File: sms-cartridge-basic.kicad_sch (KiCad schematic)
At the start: 5 parts, among them U1 27C256, U2 SMSUCartEdge

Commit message: v0.1
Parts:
- U2: footprint (none) -> MasterSystem:SMS_Cartridge
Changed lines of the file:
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@@
   (no_connect (at 216.535 57.785))
   (no_connect (at 216.535 60.325))
+  (no_connect (at 216.535 83.185))
   (no_connect (at 216.535 75.565))
   (no_connect (at 216.535 78.105))
   (no_connect (at 216.535 80.645))
-  (no_connect (at 216.535 83.185))
   (no_connect (at 216.535 67.945))
   (no_connect (at 216.535 70.485))
@@
       (effects (font (size 1.27 1.27)) (justify left))
     )
-    (property "Footprint" "" (id 2) (at 205.105 52.705 0)
+    (property "Footprint" "MasterSystem:SMS_Cartridge" (id 2) (at 205.105 52.705 0)
       (effects (font (size 1.27 1.27)) hide)
     )
@@
     )
     (path "/cae6533d-13d3-4f9b-a8e3-e699bd050290"
-      (reference "U2") (unit 1) (value "SMSUCartEdge") (footprint "")
-    )
-  )
+      (reference "U2") (unit 1) (value "SMSUCartEdge") (footprint "MasterSystem:SMS_Cartridge")
+    )
+  )

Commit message: Bodge to M0-7
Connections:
- net ~{M0-7}: now reaches U2.11 (~{M0-7})
- net ~{M0-7}: now also U1.22 (~{OE})
- net ~{RD}: no longer names the net of U2.4 (~{RD})
- net ~{RD}: no longer U1.22 (~{OE})
- no-connect marks 16 -> 19
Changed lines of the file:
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@@
   (junction (at 210.185 137.795) (diameter 0) (color 0 0 0 0)
   )
+  (no_connect (at 216.535 106.045))
+  (no_connect (at 216.535 103.505))
+  (no_connect (at 216.535 100.965))
   (no_connect (at 216.535 108.585))
   (no_connect (at 216.535 57.785))
@@
     (stroke (width 0) (type default) (color 0 0 0 0))
   )
+  (wire (pts (xy 216.535 98.425) (xy 222.885 98.425))
+    (stroke (width 0) (type default) (color 0 0 0 0))
+  )
   (wire (pts (xy 196.85 100.965) (xy 198.755 100.965))
     (stroke (width 0) (type default) (color 0 0 0 0))
@@
     (stroke (width 0) (type default) (color 0 0 0 0))
   )
-  (wire (pts (xy 216.535 106.045) (xy 222.885 106.045))
-    (stroke (width 0) (type default) (color 0 0 0 0))
-  )
   (wire (pts (xy 216.535 95.885) (xy 222.885 95.885))
     (stroke (width 0) (type default) (color 0 0 0 0))
@@
     (effects (font (size 1.27 1.27)) (justify right bottom))
   )
+  (label "~{M0-7}" (at 88.9 99.06 180)
+    (effects (font (size 1.27 1.27)) (justify right bottom))
+  )
   (label "a7" (at 95.25 71.12 180)
     (effects (font (size 1.27 1.27)) (justify right bottom))
@@
     (effects (font (size 1.27 1.27)) (justify right bottom))
   )
-  (label "~{RD}" (at 222.885 106.045 0)
-    (effects (font (size 1.27 1.27)) (justify left bottom))
-  )
   (label "a4" (at 196.85 90.805 180)
     (effects (font (size 1.27 1.27)) (justify right bottom))
@@
     (effects (font (size 1.27 1.27)) (justify right bottom))
   )
-  (label "~{RD}" (at 88.9 99.06 180)
-    (effects (font (size 1.27 1.27)) (justify right bottom))
-  )
   (label "a13" (at 95.25 86.36 180)
     (effects (font (size 1.27 1.27)) (justify right bottom))
@@
     (effects (font (size 1.27 1.27)) (justify right bottom))
   )
+  (label "~{M0-7}" (at 222.885 98.425 0)
+    (effects (font (size 1.27 1.27)) (justify left bottom))
+  )
   (label "a1" (at 196.85 83.185 180)

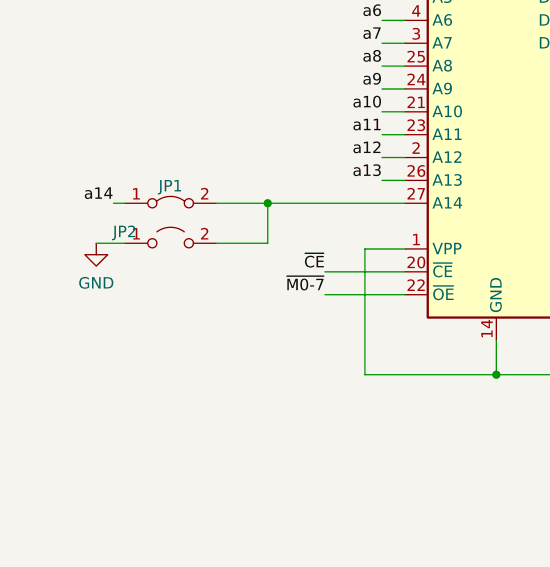
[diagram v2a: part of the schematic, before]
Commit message: 27c64 support
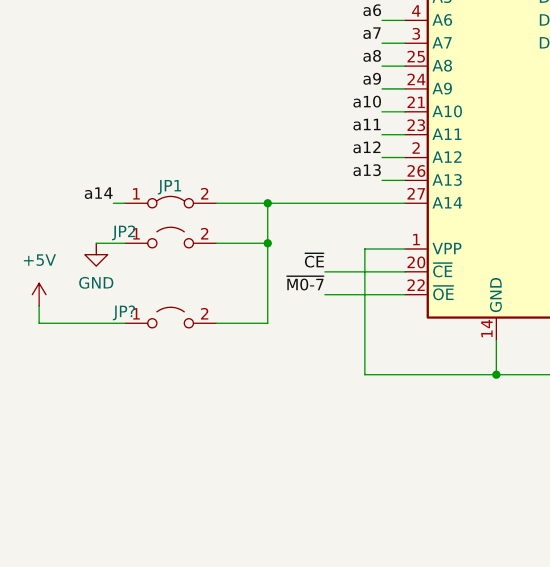
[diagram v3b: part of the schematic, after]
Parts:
- added JP?: Jumper_2_Open, Jumper:SolderJumper-2_P1.3mm_Open_RoundedPad1.0x1.5mm, symbol Jumper:Jumper_2_Open
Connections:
- net +5V: now also JP?.1 (A)
- net at JP1.2 (B), JP2.2 (B), U1.27 (A14): now also JP?.2 (B)
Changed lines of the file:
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@@
   (junction (at 82.55 88.9) (diameter 0) (color 0 0 0 0)
+  )
+  (junction (at 82.55 93.345) (diameter 0) (color 0 0 0 0)
   )
   (junction (at 206.375 36.83) (diameter 0) (color 0 0 0 0)
@@
     (stroke (width 0) (type default) (color 0 0 0 0))
   )
+  (wire (pts (xy 57.15 102.235) (xy 66.675 102.235))
+    (stroke (width 0) (type default) (color 0 0 0 0))
+  )
   (wire (pts (xy 203.835 36.83) (xy 206.375 36.83))
     (stroke (width 0) (type default) (color 0 0 0 0))
@@
     (stroke (width 0) (type default) (color 0 0 0 0))
   )
+  (wire (pts (xy 76.835 102.235) (xy 82.55 102.235))
+    (stroke (width 0) (type default) (color 0 0 0 0))
+  )
   (wire (pts (xy 212.725 144.145) (xy 212.725 137.795))
     (stroke (width 0) (type default) (color 0 0 0 0))
@@
     (stroke (width 0) (type default) (color 0 0 0 0))
   )
+  (wire (pts (xy 57.15 100.33) (xy 57.15 102.235))
+    (stroke (width 0) (type default) (color 0 0 0 0))
+  )
   (wire (pts (xy 205.105 137.795) (xy 205.105 131.445))
     (stroke (width 0) (type default) (color 0 0 0 0))
@@
     (stroke (width 0) (type default) (color 0 0 0 0))
   )
+  (wire (pts (xy 82.55 102.235) (xy 82.55 93.345))
+    (stroke (width 0) (type default) (color 0 0 0 0))
+  )
   (wire (pts (xy 196.85 62.865) (xy 198.755 62.865))
     (stroke (width 0) (type default) (color 0 0 0 0))
@@
   (label "a5" (at 95.25 66.04 180)
     (effects (font (size 1.27 1.27)) (justify right bottom))
+  )
+  (symbol (lib_id "power:+5V") (at 57.15 100.33 0) (unit 1)
+    (in_bom yes) (on_board yes) (fields_autoplaced)
+    (property "Reference" "#PWR?" (id 0) (at 57.15 104.14 0)
+      (effects (font (size 1.27 1.27)) hide)
+    )
+    (property "Value" "+5V" (id 1) (at 57.15 95.25 0))
+    (property "Footprint" "" (id 2) (at 57.15 100.33 0)
+      (effects (font (size 1.27 1.27)) hide)
+    )
+    (property "Datasheet" "" (id 3) (at 57.15 100.33 0)
+      (effects (font (size 1.27 1.27)) hide)
+    )
+    (pin "1")
   )
   (symbol (lib_id "Jumper:Jumper_2_Bridged") (at 71.755 88.9 0) (unit 1)
@@
     )
     (property "Datasheet" "~" (id 3) (at 187.96 141.605 0)
+      (effects (font (size 1.27 1.27)) hide)
+    )
+    (pin "1")
+    (pin "2")
+  )
+  (symbol (lib_id "Jumper:Jumper_2_Open") (at 71.755 102.235 0) (unit 1)
+    (in_bom yes) (on_board yes)
+    (property "Reference" "JP?" (id 0) (at 66.675 100.965 0))
+    (property "Value" "Jumper_2_Open" (id 1) (at 71.755 97.79 0)
+      (effects (font (size 1.27 1.27)) hide)
+    )
+    (property "Footprint" "Jumper:SolderJumper-2_P1.3mm_Open_RoundedPad1.0x1.5mm" (id 2) (at 71.755 102.235 0)
+      (effects (font (size 1.27 1.27)) hide)
+    )
+    (property "Datasheet" "~" (id 3) (at 71.755 102.235 0)
       (effects (font (size 1.27 1.27)) hide)
     )
@@
       (reference "#PWR0107") (unit 1) (value "GND") (footprint "")
     )
+    (path "/03d42a6b-ada2-4bb7-928c-6aa31dfe4e1c"
+      (reference "#PWR?") (unit 1) (value "+5V") (footprint "")
+    )
     (path "/60a45626-6ba1-4c8e-b9bd-86b6decf0cc0"
       (reference "C1") (unit 1) (value "0.1µF") (footprint "Capacitor_THT:C_Disc_D3.8mm_W2.6mm_P2.50mm")
@@
       (reference "JP2") (unit 1) (value "Jumper_2_Open") (footprint "Jumper:SolderJumper-2_P1.3mm_Open_RoundedPad1.0x1.5mm")
     )
+    (path "/640120f3-2e43-4994-868f-d521a3b9a66b"
+      (reference "JP?") (unit 1) (value "Jumper_2_Open") (footprint "Jumper:SolderJumper-2_P1.3mm_Open_RoundedPad1.0x1.5mm")
+    )
     (path "/757a0c1f-47da-44f3-a5e7-2bebc114b1da"

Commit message: Update schematic
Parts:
- gave numbers to parts that had none: 1
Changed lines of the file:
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@@
   (symbol (lib_id "power:+5V") (at 57.15 100.33 0) (unit 1)
     (in_bom yes) (on_board yes) (fields_autoplaced)
-    (property "Reference" "#PWR?" (id 0) (at 57.15 104.14 0)
+    (property "Reference" "#PWR0108" (id 0) (at 57.15 104.14 0)
       (effects (font (size 1.27 1.27)) hide)
     )
@@
   (symbol (lib_id "Jumper:Jumper_2_Open") (at 71.755 102.235 0) (unit 1)
     (in_bom yes) (on_board yes)
-    (property "Reference" "JP?" (id 0) (at 66.675 100.965 0))
+    (property "Reference" "JP3" (id 0) (at 66.675 100.965 0))
     (property "Value" "Jumper_2_Open" (id 1) (at 71.755 97.79 0)
       (effects (font (size 1.27 1.27)) hide)
@@
     )
     (path "/03d42a6b-ada2-4bb7-928c-6aa31dfe4e1c"
-      (reference "#PWR?") (unit 1) (value "+5V") (footprint "")
+      (reference "#PWR0108") (unit 1) (value "+5V") (footprint "")
     )
     (path "/60a45626-6ba1-4c8e-b9bd-86b6decf0cc0"
@@
     )
     (path "/640120f3-2e43-4994-868f-d521a3b9a66b"
-      (reference "JP?") (unit 1) (value "Jumper_2_Open") (footprint "Jumper:SolderJumper-2_P1.3mm_Open_RoundedPad1.0x1.5mm")
+      (reference "JP3") (unit 1) (value "Jumper_2_Open") (footprint "Jumper:SolderJumper-2_P1.3mm_Open_RoundedPad1.0x1.5mm")
     )
     (path "/757a0c1f-47da-44f3-a5e7-2bebc114b1da"
